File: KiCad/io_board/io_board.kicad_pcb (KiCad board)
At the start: 4 copper layers, 131.1 x 99.1 mm, 83 parts, among them J1 RS232, J2 Keyboard, J3 SD_Card, J4 JTAG, J5 DS1307, J6 BME280, J7 I²C, U1 ST16C550CJ44, U10 74HC367, U11 74HC367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

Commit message: Updated I/O board
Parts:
- removed U8: 74HC245, Package_SO:SOIC-20W_7.5x12.8mm_P1.27mm
- added C41: 100n, Capacitor_SMD:C_1206_3216Metric, B.Cu at (131.4, 147.4)
- added R14: 1K, Resistor_SMD:R_1206_3216Metric, F.Cu at (76.5, 117.7)
- added R15: 2K2, Resistor_SMD:R_1206_3216Metric, B.Cu at (113.7, 102.6)
- added R16: 4K7, Resistor_SMD:R_1206_3216Metric, B.Cu at (143.6, 130.8)
- added R17: 4K7, Resistor_SMD:R_1206_3216Metric, B.Cu at (139.8, 143.8)
- added R18: 4K7, Resistor_SMD:R_1206_3216Metric, B.Cu at (143.6, 127.6)
- added R19: 4K7, Resistor_SMD:R_1206_3216Metric, B.Cu at (139.8, 146.3)
- C10: value 100n -> 47µ; footprint Capacitor_SMD:C_1206_3216Metric -> Capacitor_SMD:CP_Elec_5x5.4; moved to F.Cu
- C17: footprint Capacitor_THT:CP_Radial_D5.0mm_P2.50mm -> Capacitor_SMD:CP_Elec_5x5.4
- C28, R6: moved to B.Cu
- R12, R13: value 270 -> 100; moved to F.Cu
- X2: value 10 MHz -> 20 MHz; footprint Oscillator:Oscillator_DIP-14 -> Oscillator:Oscillator_SMD_Abracon_ASV-4Pin_7.0x5.1mm
- moved R9 37.1 mm to (123.8, 137.7)
- moved R8 31.3 mm to (123.8, 134.5)
- moved J4 30.7 mm to (127.9, 146.2), turned to 270 degrees
- moved R7 23.6 mm to (125.9, 130.2)
- moved R6 16.2 mm to (139.8, 139.6), turned to 180 degrees
- moved C28 9.98 mm to (139.8, 137.0), turned to 0 degrees
- moved C18 9.68 mm to (139.2, 126.7), turned to 90 degrees
- moved C10 4.34 mm to (130.7, 138.0)
- moved X2 3.89 mm to (124.2, 118.7)
- moved C17 3.51 mm to (76.9, 146.1)
- moved R13 3.50 mm to (149.5, 116.8)
- moved R12 3.34 mm to (149.5, 119.9)
- moved C39 2.45 mm to (124.1, 118.7), turned to 0 degrees
- moved J5 1.78 mm to (123.6, 91.4)
- moved X1 0.25 mm to (35.3, 147.3)
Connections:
- net /SD drive/~WR_BUFFER_3 renamed /SD drive/~CS_BUFFER_3
- net Net-(R12-Pad1) renamed /SD drive/LD_GN
- net Net-(R13-Pad1) renamed /SD drive/LD_RD
- net Net-(U1-Pad10) renamed /serial/RCLK
- net Net-(U1-Pad11) renamed /serial/RX_5
- net Net-(U1-Pad13) renamed /serial/TX_5
- net Net-(U1-Pad36) renamed /serial/RTS_5
- net Net-(U1-Pad40) renamed /serial/CTS_5
- net Net-(U17-Pad1) renamed /I2C/I2C_D0
- net Net-(U17-Pad2) renamed /I2C/I2C_D1
- net Net-(U17-Pad3) renamed /I2C/I2C_D2
- net Net-(U17-Pad4) renamed /I2C/I2C_D3
- net Net-(U17-Pad5) renamed /I2C/I2C_D4
- net Net-(U17-Pad6) renamed /I2C/I2C_D5
- net Net-(U17-Pad7) renamed /I2C/I2C_D6
- net Net-(U17-Pad8) renamed /I2C/I2C_D7
- net Net-(U3-Pad3) renamed /PS2/KDATA_OUT
- net Net-(U4-Pad1) renamed /PS2/KCLK_OUT
- net Net-(U4-Pad4) renamed /PS2/~PCLK
- net ~WR_BUFFER renamed ~CS_BUFFER
- C10 pad 1: VCC -> VCC3
- C39 pad 1: VCC -> VCC3
- J2 pad 1: /PS2/KBD_DATA -> /PS2/KBD_CLK
- J2 pad 2: Net-(J2-Pad2) -> GND
- J2 pad 3: GND -> /PS2/KBD_DATA
- J2 pad 4: VCC -> Net-(J2-Pad4)
- J2 pad 5: /PS2/KBD_CLK -> VCC
- J3 pad 2: /SD drive/SD_DI -> /SD drive/MOSI
- J3 pad 5: /SD drive/SD_SCLK -> /SD drive/SCLK
- J3 pad 7: /SD drive/SD_DO -> /SD drive/MISO
- U13 pad 11: /SD drive/CPLD_CLK_3 -> Net-(U13-Pad11)
- U13 pad 9: /SD drive/CPLD_CLK -> Net-(U13-Pad9)
- U14 pad 10: GND -> ~D_EN_3
- U14 pad 8: Net-(U14-Pad8) -> ~D_EN
- U14 pad 9: GND -> ~D_EN_3
- U15 pad 22: ~CS_DRIVE -> ~D_EN
- U5 pad 9: A0 -> A2
- U6 pad 1: M_~IO -> ~WR
- U6 pad 26: ~WR -> M_~IO
- U7 pad 12: /SD drive/CPLD_CLK_3 -> CPLD_CLK
- U7 pad 2: /SD drive/~RESET_3 -> Net-(U7-Pad2)
- U7 pad 40: Net-(U7-Pad40) -> ~D_EN_3
- U7 pad 41: Net-(U7-Pad41) -> /SD drive/D0_3
- U7 pad 42: /SD drive/D0_3 -> /SD drive/D1_3
- U7 pad 43: /SD drive/D1_3 -> /SD drive/D2_3
- U7 pad 44: /SD drive/D2_3 -> /SD drive/~RESET_3
- U7 pad 64: /SD drive/SD_CS -> Net-(U7-Pad64)
- U7 pad 66: /SD drive/SD_DI -> Net-(U7-Pad66)
- U7 pad 67: /SD drive/SD_SCLK -> Net-(U7-Pad67)
- U7 pad 68: /SD drive/SD_DO -> Net-(U7-Pad68)
- U7 pad 70: Net-(U7-Pad70) -> /SD drive/SD_CS
- U7 pad 71: Net-(U7-Pad71) -> /SD drive/MOSI
- U7 pad 72: Net-(U7-Pad72) -> /SD drive/SCLK
- U7 pad 73: Net-(U7-Pad73) -> /SD drive/MISO
- X1 pad 34: Net-(X1-Pad34) -> SCL
- X1 pad 70: Net-(X1-Pad70) -> SDA
- X2 pad 1: VCC -> VCC3
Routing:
- net SCL: track 52.5 -> 144.9 mm, vias 1 -> 2
- net SDA: track 50.4 -> 142.2 mm, vias 1 -> 2
- net VCC3: track 362.8 -> 454.1 mm, vias 18 -> 20
- net VCC: track 652.0 -> 568.2 mm
- net ~D_EN: track 0.00 -> 82.4 mm, vias 0 -> 4
- net ~D_EN_3: track 0.00 -> 76.3 mm, vias 0 -> 4
- net /SD drive/SD misc/~ACC_BUFFER: track 91.6 -> 34.9 mm, vias 5 -> 3
- net /SD drive/SD_DI: track 37.8 -> 0.00 mm, vias 2 -> 0
- net RD7: track 78.2 -> 41.4 mm
- net RD6: track 74.4 -> 38.4 mm
- net /SD drive/CPLD_CLK: track 34.7 -> 0.00 mm, vias 1 -> 0
- net /SD drive/TDI: track 75.7 -> 41.2 mm
- net RD5: track 74.2 -> 40.6 mm
- net ~RD: track 274.4 -> 241.4 mm, vias 9 -> 7
- net RD4: track 75.2 -> 43.9 mm
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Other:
- board text added: "20 MHz"
- board text added: "8042"
- board text added: "Rev. 1.0 2021"
- board text added: "UART"
- board text removed: "10 MHz"
- board text removed: "Rev. 1.0 2020"

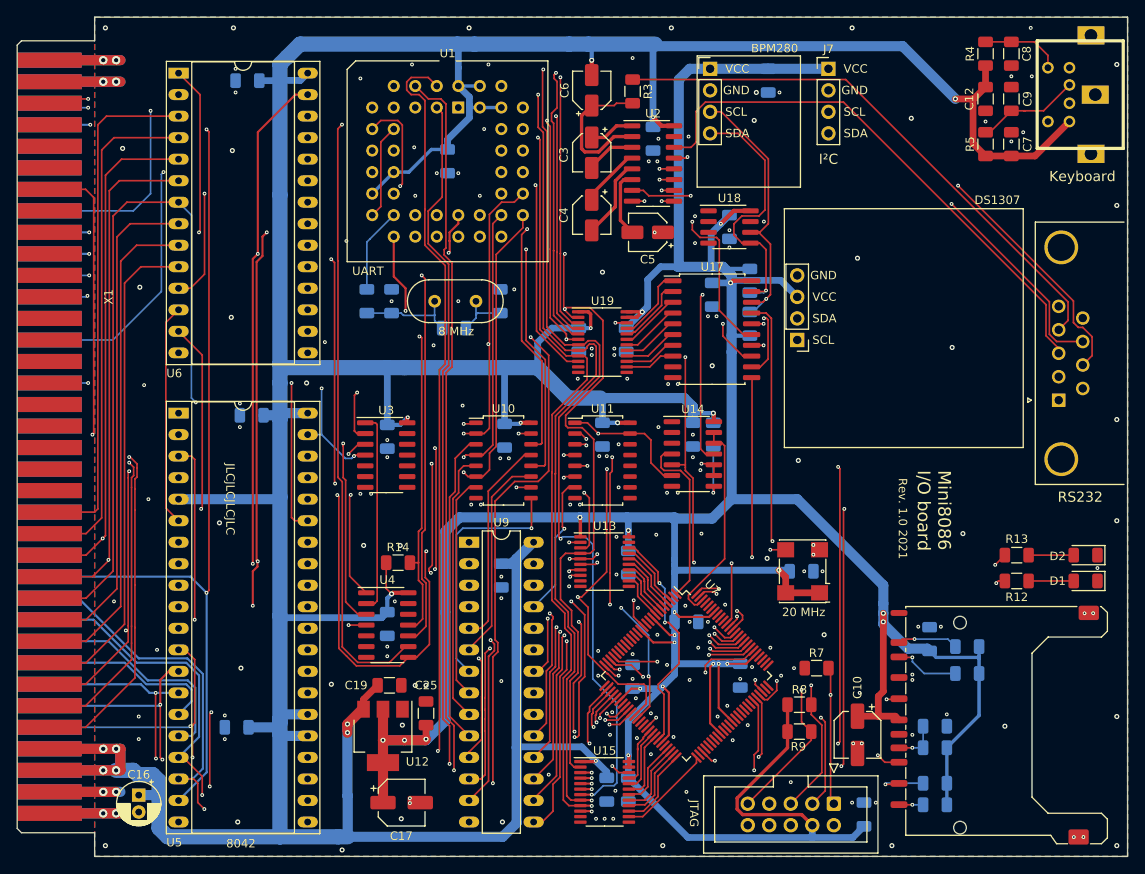
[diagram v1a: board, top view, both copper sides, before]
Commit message: Updated KiCad versioning information in schematics. Fixed button wrong pinout in backplane. Added missing files to git.
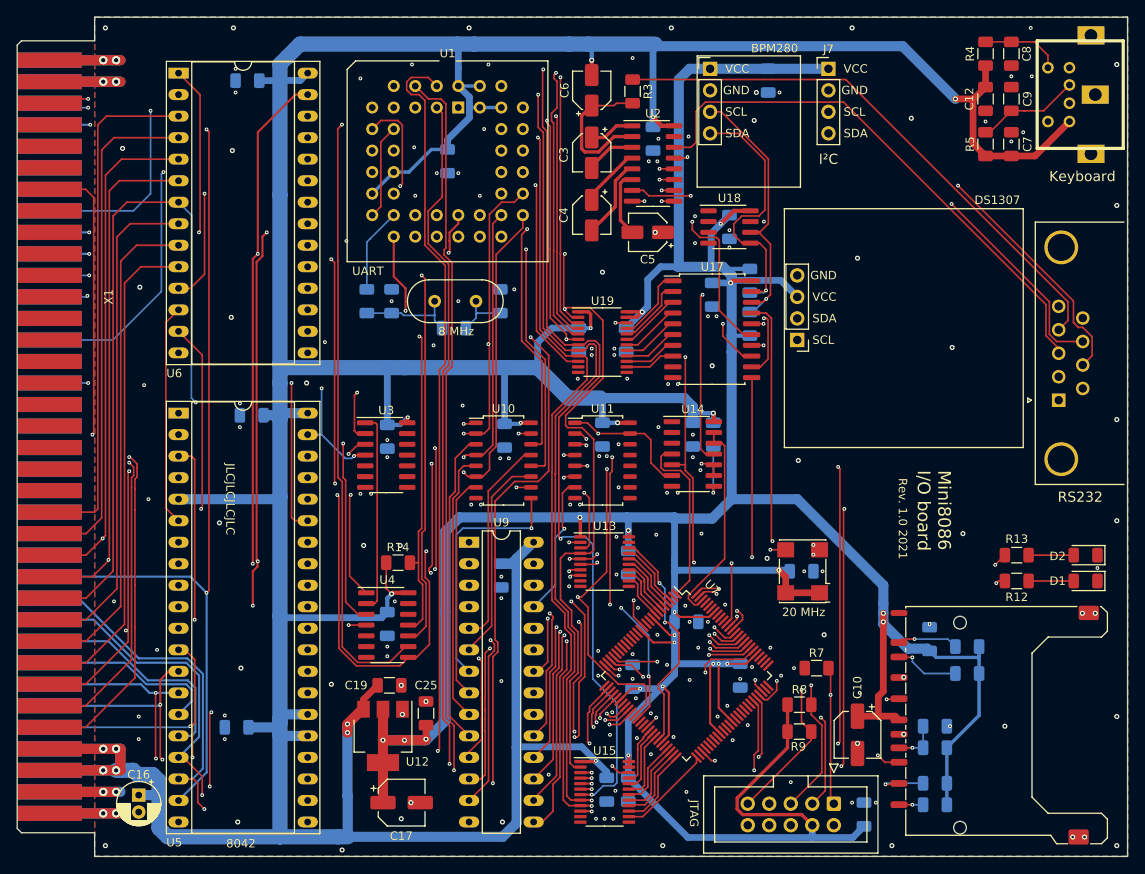
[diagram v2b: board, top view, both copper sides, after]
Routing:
- net GND: vias 194 -> 190
